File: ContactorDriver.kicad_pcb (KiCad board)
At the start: 2 copper layers, 37 x 49 mm, 32 parts, among them J1 PowerConn, J2 DashboardConnA, J3 ContactorAConn, J4 FanConn1, J5 FanConn2, J6 DashboardConnB, J7 ContactorBConn, J8 FanConn3, Q1 IRLML0030TRPbF, Q2 IRLML0030TRPbF, Q3 IRLML0030TRPbF

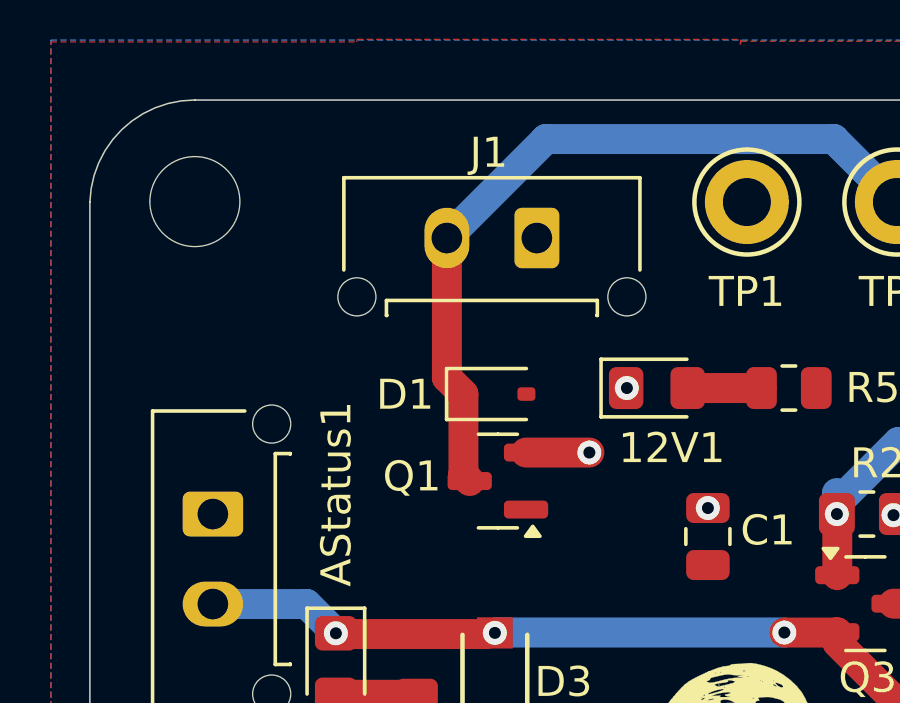
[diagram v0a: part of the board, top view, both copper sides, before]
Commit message: Fixed spoke width + input power pour
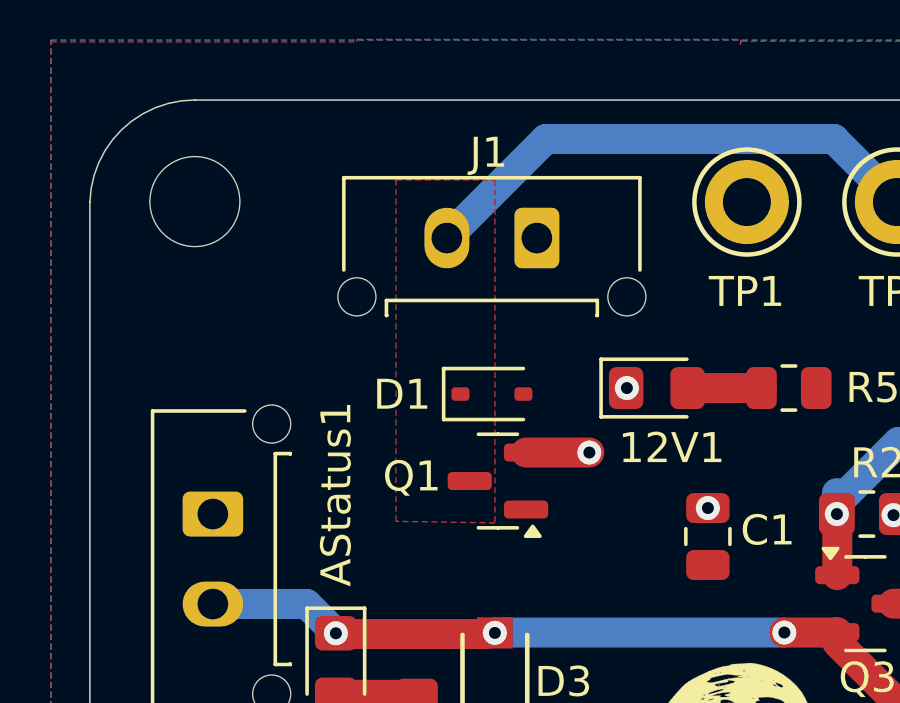
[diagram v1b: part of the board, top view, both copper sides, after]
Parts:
- moved D1 0.10 mm to (110.0, 73.4)
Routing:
- net Net-(D1-A1): track 25.7 -> 17.2 mm
- added copper zone on F.Cu, net Net-(D1-A1)
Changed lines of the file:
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@@
 		(tags "LED handsolder")
 		(property "Reference" "BStatus1"
-			(at -5.589 -0.124 270)
+			(at -5.589 -0.124 -90)
 			(layer "F.SilkS")
 			(effects
@@
 	(footprint "Diode_SMD:D_SOD-323"
 		(layer "F.Cu")
-		(at 110.105 73.44)
+		(at 110.0066 73.44)
 		(descr "SOD-323")
 		(tags "SOD-323")
@@
 	)
 	(segment
-		(start 109.055 76.1275)
-		(end 109.2675 76.34)
-		(width 1)
-		(layer "F.Cu")
-		(net 3)
-	)
-	(segment
-		(start 109.055 73.44)
-		(end 109.055 76.1275)
-		(width 1)
-		(layer "F.Cu")
-		(net 3)
-	)
-	(segment
-		(start 108.505 72.89)
-		(end 109.055 73.44)
-		(width 1)
-		(layer "F.Cu")
-		(net 3)
-	)
-	(segment
-		(start 108.505 68.24)
-		(end 108.505 72.89)
-		(width 1)
-		(layer "F.Cu")
-		(net 3)
-	)
-	(segment
 		(start 111.805 64.94)
 		(end 121.405 64.94)
@@
 		(fill yes
 			(thermal_gap 0.5)
-			(thermal_bridge_width 0.5)
+			(thermal_bridge_width 1)
 		)
 		(polygon
@@
 	)
 	(zone
+		(net 3)
+		(net_name "Net-(D1-A1)")
+		(layer "F.Cu")
+		(hatch edge 0.5)
+		(priority 2)
+		(connect_pads
+			(clearance 0.2)
+		)
+		(min_thickness 0.25)
+		(filled_areas_thickness no)
+		(fill yes
+			(thermal_gap 0.5)
+			(thermal_bridge_width 2)
+		)
+		(polygon
+			(pts
+				(xy 106.8062 66.3052) (xy 110.1082 66.3052) (xy 110.1082 77.7352) (xy 106.8062 77.6844)
+			)
+		)
+	)
+	(zone
 		(net 2)
 		(net_name "GND")
@@
 		(fill yes
 			(thermal_gap 0.5)
-			(thermal_bridge_width 0.5)
+			(thermal_bridge_width 1)
 		)
 		(polygon

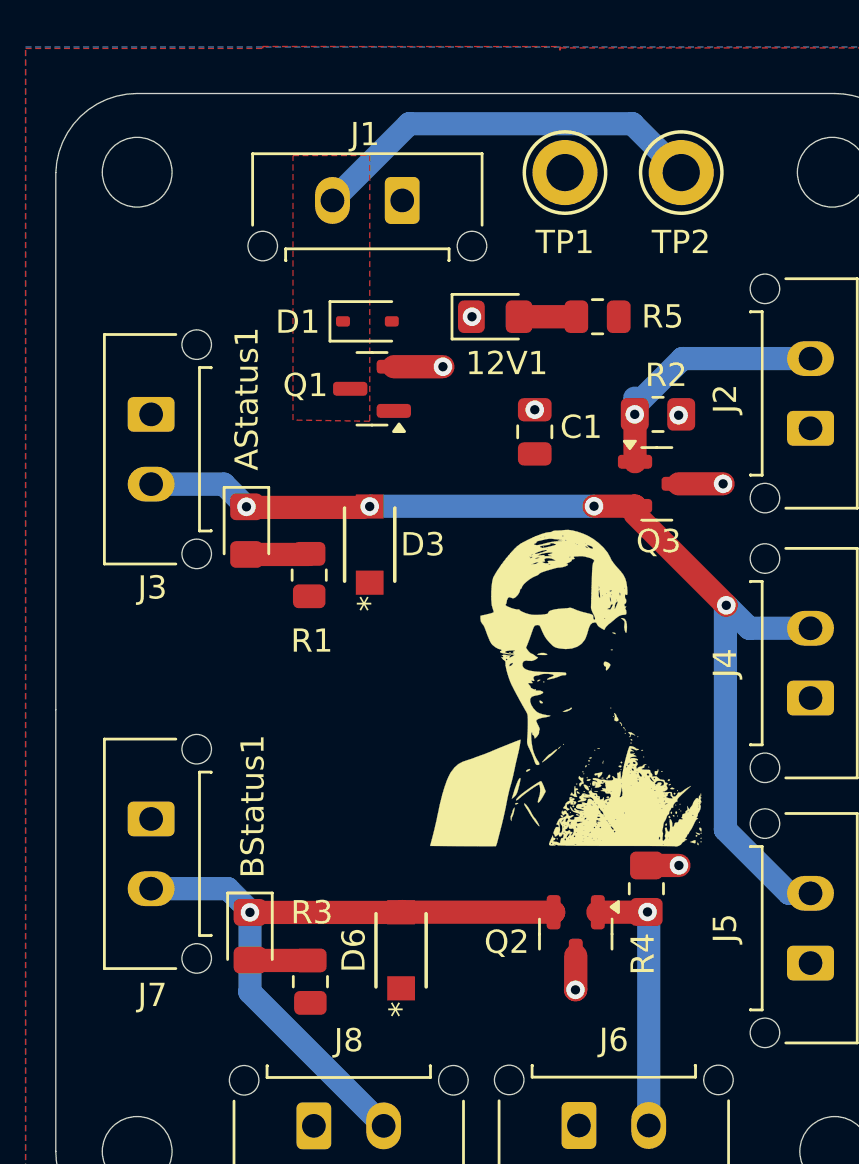
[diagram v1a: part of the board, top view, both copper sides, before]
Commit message: Changed out schottky diodes + updated changelog
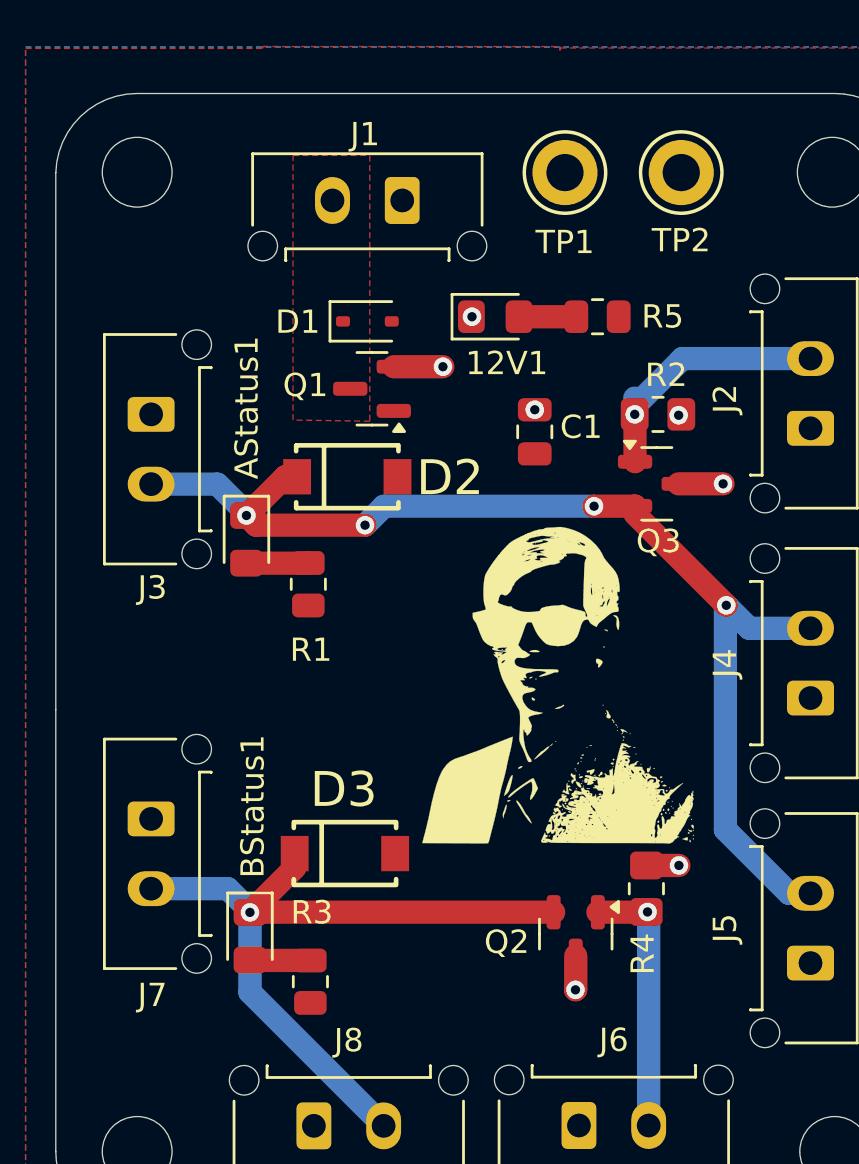
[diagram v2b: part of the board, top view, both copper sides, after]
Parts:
- removed D6: V2F22HM3/H, UTSVT_Passive:V2F22HM
- added D2: VSSAF522, UTSVT_Passive:DO-221AC, F.Cu at (109.1, 80.1)
- D3: value V2F22HM3/H -> VSSAF522; footprint UTSVT_Passive:V2F22HM -> UTSVT_Passive:DO-221AC
- TP2: value GND_UNISO -> GND
- moved D3 13.3 mm to (109.0, 96.3), turned to 0 degrees
- moved R1 0.39 mm to (107.5, 84.7)
- moved AStatus1 0.38 mm to (104.8, 82.8)
- moved LOGO1 0.36 mm to (117.7, 88.9)
- turned TP2 to 0 degrees
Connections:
- D3 pad 2: /CONTACTOR_A_V- -> /CONTACTOR_B_V-
- TP2 pad 1: Net-(D1-A1) -> GND
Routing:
- net Net-(D1-A1): track 17.2 -> 0.00 mm
- net /CONTACTOR_A_V-: track 45.0 -> 48.8 mm
- net /CONTACTOR_B_V-: track 29.3 -> 32.7 mm
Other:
- board text added: "Contactor-Driver (Daybreak Fix) By: Devin & Dylan Kretschman"

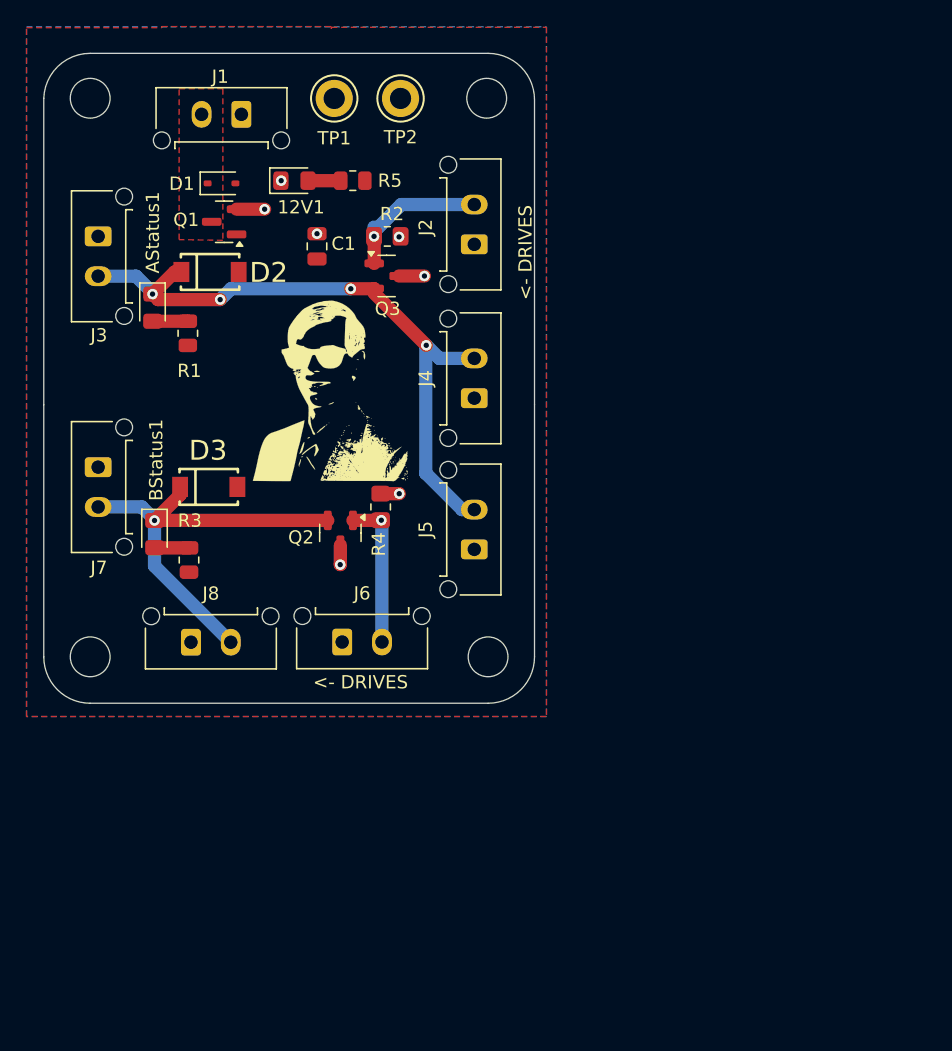
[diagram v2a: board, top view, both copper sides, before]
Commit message: Added one more contactor, and another fan conn
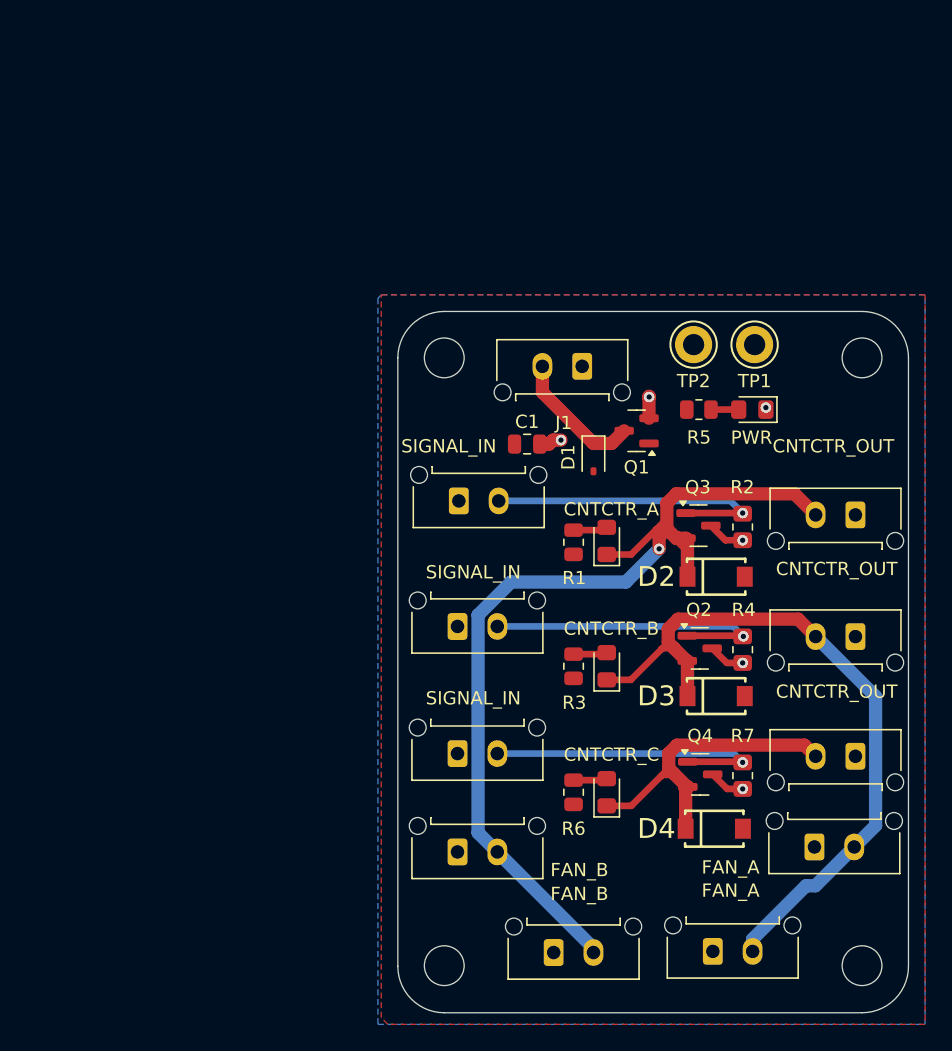
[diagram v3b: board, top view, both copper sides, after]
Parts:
- added CStatus1: Green, LED_SMD:LED_0805_2012Metric_Pad1.15x1.40mm_HandSolder, F.Cu at (139.1, 119.3)
- added D4: VSSAF522, UTSVT_Passive:DO-221AC, F.Cu at (147.2, 122.1)
- added J10: FanConn3, Connector_Molex:Molex_Micro-Fit_3.0_43650-0215_1x02_P3.00mm_Vertical, F.Cu at (154.7, 123.5)
- added J11: FanConn4, Connector_Molex:Molex_Micro-Fit_3.0_43650-0215_1x02_P3.00mm_Vertical, F.Cu at (147.1, 131.3)
- added J9: FanConn2, Connector_Molex:Molex_Micro-Fit_3.0_43650-0215_1x02_P3.00mm_Vertical, F.Cu at (135.1, 131.4)
- added Q4: IRLML0030TRPbF, Package_TO_SOT_SMD:SOT-23, F.Cu at (146.1, 118.0)
- added R6: 10k, Resistor_SMD:R_0805_2012Metric, F.Cu at (136.6, 119.3)
- added R7: 100k, Resistor_SMD:R_0805_2012Metric_Pad1.20x1.40mm_HandSolder, F.Cu at (149.3, 118.1)
- J4: value FanConn1 -> DashboardConnB
- J5: value FanConn2 -> ContactorBConn
- J6: value DashboardConnB -> DashboardConnC
- J7: value ContactorBConn -> ContactorCConn
- J8: value FanConn3 -> FanConn1
- LOGO1: moved to B.Cu
- moved H1 71.3 mm to (158.3, 132.4)
- moved H2 70.6 mm to (126.8, 132.4)
- moved H4 62.4 mm to (158.3, 86.6)
- moved J7 61.1 mm to (157.8, 116.6), turned to 180 degrees
- moved J3 60.8 mm to (157.8, 98.4), turned to 180 degrees
- moved LOGO1 47.9 mm to (144.0, 129.0), turned to 180 degrees
- moved D2 44.5 mm to (147.3, 103.1)
- moved D3 41.4 mm to (147.3, 112.1)
- moved 12V1 38.6 mm to (150.0, 90.5), turned to 180 degrees
- moved AStatus1 38.5 mm to (139.1, 100.4), turned to 90 degrees
- moved TP1 36.7 mm to (150.2, 85.6)
- moved LOGO2 35.9 mm to (146.3, 115.1), turned to 90 degrees
- moved BStatus1 35.5 mm to (139.1, 109.8), turned to 90 degrees
- moved LOGO3 35.2 mm to (139.4, 105.4)
- moved Q1 34.9 mm to (141.3, 92.1)
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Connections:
- J4 pad 2: /CONTACTOR_A_V- -> Net-(J4-Pin_2)
- J5 pad 2: /CONTACTOR_A_V- -> /CONTACTOR_B_V-
- J7 pad 2: /CONTACTOR_B_V- -> /CONTACTOR_C_V-
- J8 pad 2: /CONTACTOR_B_V- -> /CONTACTOR_A_V-
- Q2 pad 1: Net-(J6-Pin_2) -> Net-(J4-Pin_2)
- R4 pad 2: Net-(J6-Pin_2) -> Net-(J4-Pin_2)
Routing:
- net /CONTACTOR_A_V-: track 48.8 -> 74.5 mm, vias 4 -> 1
- net /CONTACTOR_C_V-: track 0.00 -> 24.9 mm
- net /CONTACTOR_B_V-: track 32.7 -> 56.2 mm, vias 1 -> 0
- net Net-(J4-Pin_2): track 0.00 -> 23.2 mm, vias 0 -> 1
- net Net-(J2-Pin_2): track 11.2 -> 23.1 mm
- net Net-(J6-Pin_2): track 11.3 -> 22.9 mm
- net Net-(D1-A1): track 0.00 -> 10.1 mm
- net GND: track 6.89 -> 11.7 mm, vias 7 -> 6
- net Net-(CStatus1-A): track 0.00 -> 2.55 mm
- removed copper zone on F.Cu, net Net-(D1-A1)
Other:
- board size 37 x 49 mm -> 38.5 x 52.9 mm
- board text added: "CNTCTR_A"
- board text added: "CNTCTR_B"
- board text added: "CNTCTR_C"
- board text added: "CNTCTR_OUT"
- board text added: "FAN_A"
- board text added: "FAN_B"
- board text added: "PWR"
- board text added: "SIGNAL_IN"
- board text removed: "<- DRIVES"

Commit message: Fixed reverse polarity protection circuitry
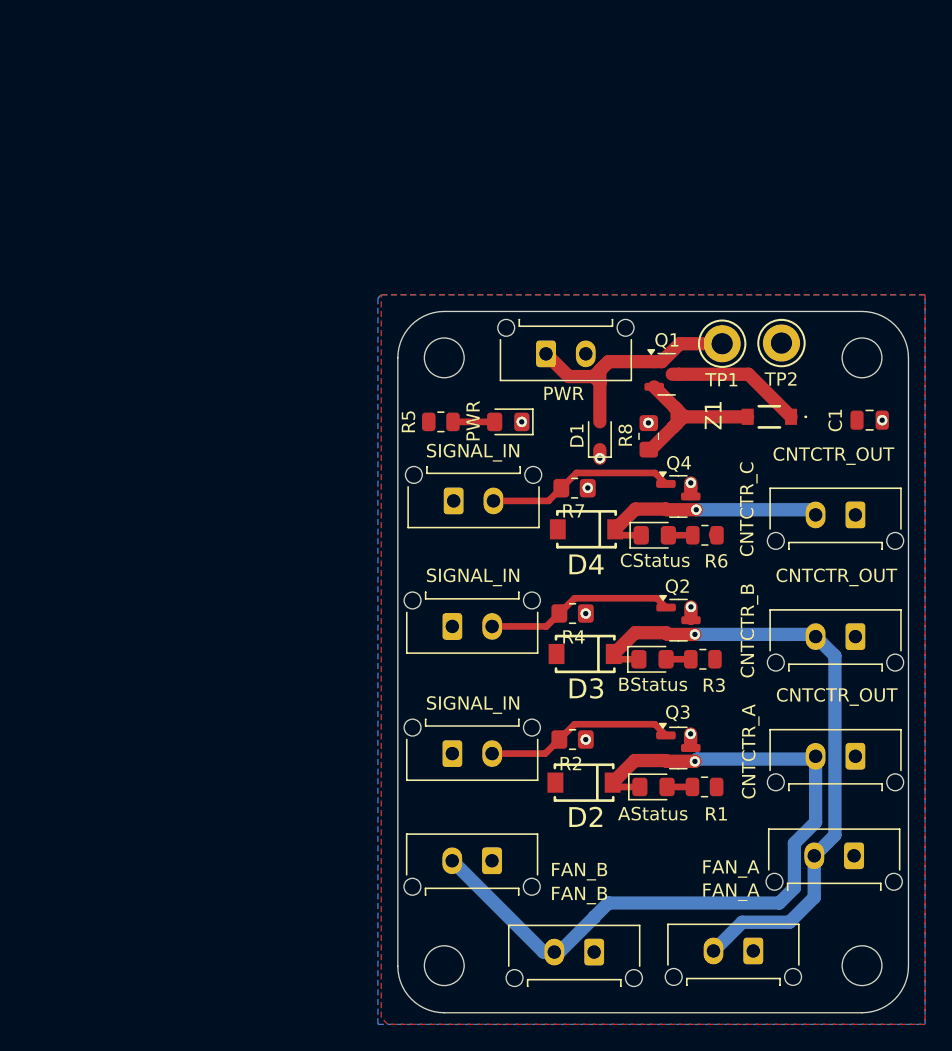
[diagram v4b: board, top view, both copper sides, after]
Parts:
- added R8: 100k, Resistor_SMD:R_0805_2012Metric_Pad1.20x1.40mm_HandSolder, F.Cu at (142.2, 92.5)
- added Z1: BZT52-B12-QX, Zener:BZT52B12QX, F.Cu at (151.3, 91.0)
- Q1: value IRLML0030TRPbF -> NDS356AP-VB
- moved C1 25.9 mm to (158.9, 91.3)
- moved R7 25.1 mm to (136.6, 96.4), turned to 180 degrees
- moved D4 24.5 mm to (137.5, 99.5), turned to 180 degrees
- moved R6 21.8 mm to (146.4, 100.0), turned to 0 degrees
- moved Q4 21.0 mm to (144.4, 97.0)
- moved R1 20.9 mm to (146.4, 119.0), turned to 0 degrees
- moved R2 20.5 mm to (136.5, 115.4), turned to 180 degrees
- moved CStatus 19.7 mm to (142.7, 100.0), turned to 0 degrees
- moved R5 19.5 mm to (126.5, 91.4)
- moved J2 19.1 mm to (127.4, 116.4)
- moved J6 19.1 mm to (127.5, 97.4)
- moved AStatus 18.9 mm to (142.6, 119.0), turned to 0 degrees
- moved D2 18.4 mm to (137.3, 118.6), turned to 180 degrees
- moved 12V1 18.4 mm to (131.6, 91.4)
- moved J3 18.2 mm to (157.8, 116.6)
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- renumbered AStatus1 to AStatus, BStatus1 to BStatus, CStatus1 to CStatus
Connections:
- D1 pad 1: Net-(D1-A1) -> GND
- D1 pad 2: +12V -> Net-(D1-A2)
- J1 pad 1: +12V -> Net-(D1-A2)
- J1 pad 2: Net-(D1-A1) -> GND
- Q1 pad 1: +12V -> Net-(D1-A2)
- Q1 pad 2: GND -> Net-(Q1-G)
- Q1 pad 3: Net-(D1-A1) -> +12V
- TP1 pad 1: +12V -> Net-(D1-A2)
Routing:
- net Net-(D1-A2): track 0.00 -> 20.5 mm
- net /CONTACTOR_A_V-: track 74.5 -> 59.6 mm
- net Net-(Q1-G): track 0.00 -> 13.4 mm
- net +12V: track 0.00 -> 11.6 mm
- net Net-(D1-A1): track 10.1 -> 0.00 mm
- net Net-(J4-Pin_2): track 23.2 -> 14.3 mm, vias 1 -> 0
- net Net-(J2-Pin_2): track 23.1 -> 14.4 mm, vias 1 -> 0
- net Net-(J6-Pin_2): track 22.9 -> 14.2 mm, vias 1 -> 0
- net /CONTACTOR_B_V-: track 56.2 -> 48.2 mm, vias 0 -> 1
- net GND: track 11.7 -> 4.52 mm, vias 6 -> 10
- net /CONTACTOR_C_V-: track 24.9 -> 18.1 mm, vias 0 -> 1
- net Net-(12V1-A): track 2.09 -> 3.14 mm
- net Net-(CStatus1-A): track 2.55 -> 1.84 mm
- net Net-(BStatus1-A): track 2.55 -> 1.86 mm
- net Net-(AStatus1-A): track 2.59 -> 1.91 mm
